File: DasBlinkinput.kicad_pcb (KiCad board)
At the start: 4 copper layers, 25.4 x 50.8 mm, 30 parts, among them P101 CONN_01X02, P102 CONN_01X01, P103 CONN_01X01, P104 CONN_01X01, P105 CONN_01X05, U101 LP2980, U201 MCP6404, U202 LM339

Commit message: added labels to silkscreen
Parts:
- REF V: renamed from P104
- renumbered P102 to +3V, P103 to GND, P101 to PWR
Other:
- board text added: "CH 1"
- board text added: "CH 2"
- board text added: "CH 3"
- board text added: "CH 4"
- board text added: "GND"
- board text added: "Input Voltage: +2V to +16V"
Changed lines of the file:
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@@
 (kicad_pcb (version 4) (host pcbnew 4.0.2-stable)
   (general
-    (links 0)
+    (links 70)
     (no_connects 0)
-    (area 130.480999 65.710999 156.031001 116.661001)
+    (area 130.480999 62.909666 158.502134 119.589333)
     (thickness 1.6)
-    (drawings 5)
+    (drawings 15)
     (tracks 249)
     (zones 0)
@@
     (tags "capacitor 0805")
     (attr smd)
-    (fp_text reference C203 (at 0.254 -1.778 180) (layer B.SilkS)
+    (fp_text reference C203 (at -0.0508 1.8288 180) (layer B.SilkS)
       (effects (font (size 1 1) (thickness 0.15)) (justify mirror))
     )
@@
     (tags "capacitor 0805")
     (attr smd)
-    (fp_text reference C301 (at 0 -1.397 180) (layer F.SilkS)
+    (fp_text reference C301 (at 0 -1.778 180) (layer F.SilkS)
       (effects (font (size 1 1) (thickness 0.15)))
     )
@@
     (descr "Through hole pin header")
     (tags "pin header")
-    (fp_text reference P101 (at 0.0508 -3.4544 180) (layer F.SilkS)
+    (fp_text reference PWR (at 1.143 -3.429 180) (layer F.SilkS)
       (effects (font (size 1 1) (thickness 0.15)))
     )
@@
     (descr "Through hole pin header")
     (tags "pin header")
-    (fp_text reference P102 (at 0 -2.794) (layer F.SilkS)
+    (fp_text reference +3V (at 0 -2.794) (layer F.SilkS)
       (effects (font (size 1 1) (thickness 0.15)))
     )
@@
     (descr "Through hole pin header")
     (tags "pin header")
-    (fp_text reference P103 (at 0 -2.794) (layer F.SilkS)
+    (fp_text reference GND (at -3.556 -0.254) (layer F.SilkS)
       (effects (font (size 1 1) (thickness 0.15)))
     )
@@
     (descr "Through hole pin header")
     (tags "pin header")
-    (fp_text reference P104 (at 3.8608 -0.254 270) (layer F.SilkS)
+    (fp_text reference "REF V" (at 4.191 -0.2286 270) (layer F.SilkS)
       (effects (font (size 1 1) (thickness 0.15)))
     )
@@
     )
   )
+  (gr_text "Input Voltage:\n+2V to +16V" (at 140.843 78.232) (layer B.SilkS)
+    (effects (font (size 1.5 1.5) (thickness 0.3)) (justify mirror))
+  )
+  (gr_text "CH 4" (at 134.366 114.046) (layer F.SilkS)
+    (effects (font (size 1.5 1.5) (thickness 0.3)))
+  )
+  (gr_text "CH 3" (at 134.493 92.837) (layer F.SilkS)
+    (effects (font (size 1.5 1.5) (thickness 0.3)))
+  )
+  (gr_text "CH 2" (at 136.398 90.17) (layer F.SilkS)
+    (effects (font (size 1.5 1.5) (thickness 0.3)))
+  )
+  (gr_text "CH 1" (at 135.255 76.454) (layer F.SilkS)
+    (effects (font (size 1.5 1.5) (thickness 0.3)))
+  )
+  (gr_text "CH 4" (at 146.05 109.474 90) (layer F.SilkS)
+    (effects (font (size 1.5 1.5) (thickness 0.3)))
+  )
+  (gr_text "CH 3" (at 148.59 109.474 90) (layer F.SilkS)
+    (effects (font (size 1.5 1.5) (thickness 0.3)))
+  )
+  (gr_text "CH 2" (at 151.13 109.474 90) (layer F.SilkS)
+    (effects (font (size 1.5 1.5) (thickness 0.3)))
+  )
+  (gr_text "CH 1" (at 153.67 109.474 90) (layer F.SilkS)
+    (effects (font (size 1.5 1.5) (thickness 0.3)))
+  )
+  (gr_text GND (at 143.256 109.982 90) (layer F.SilkS)
+    (effects (font (size 1.5 1.5) (thickness 0.3)))
+  )
   (gr_line (start 130.556 116.586) (end 155.956 116.586) (angle 90) (layer Edge.Cuts) (width 0.15))

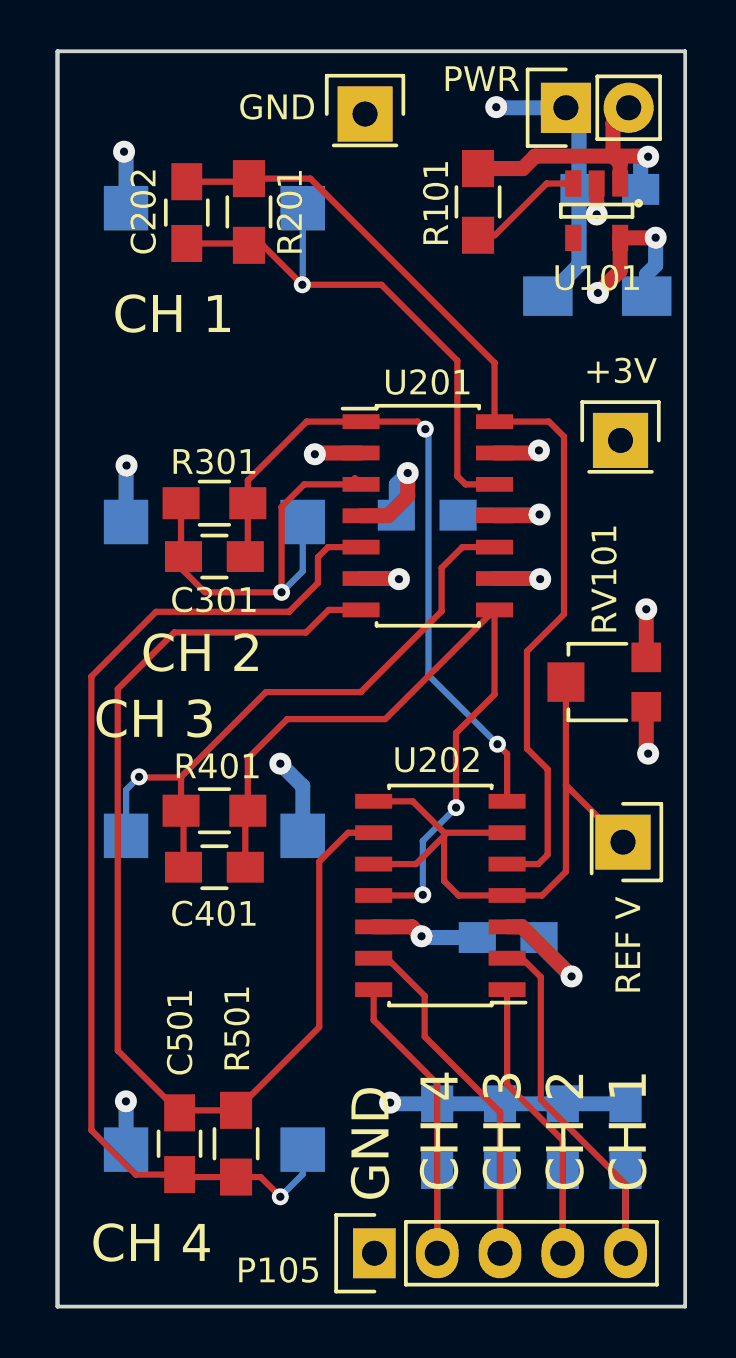
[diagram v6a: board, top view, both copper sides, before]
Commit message: added test points at outputs of op-amps
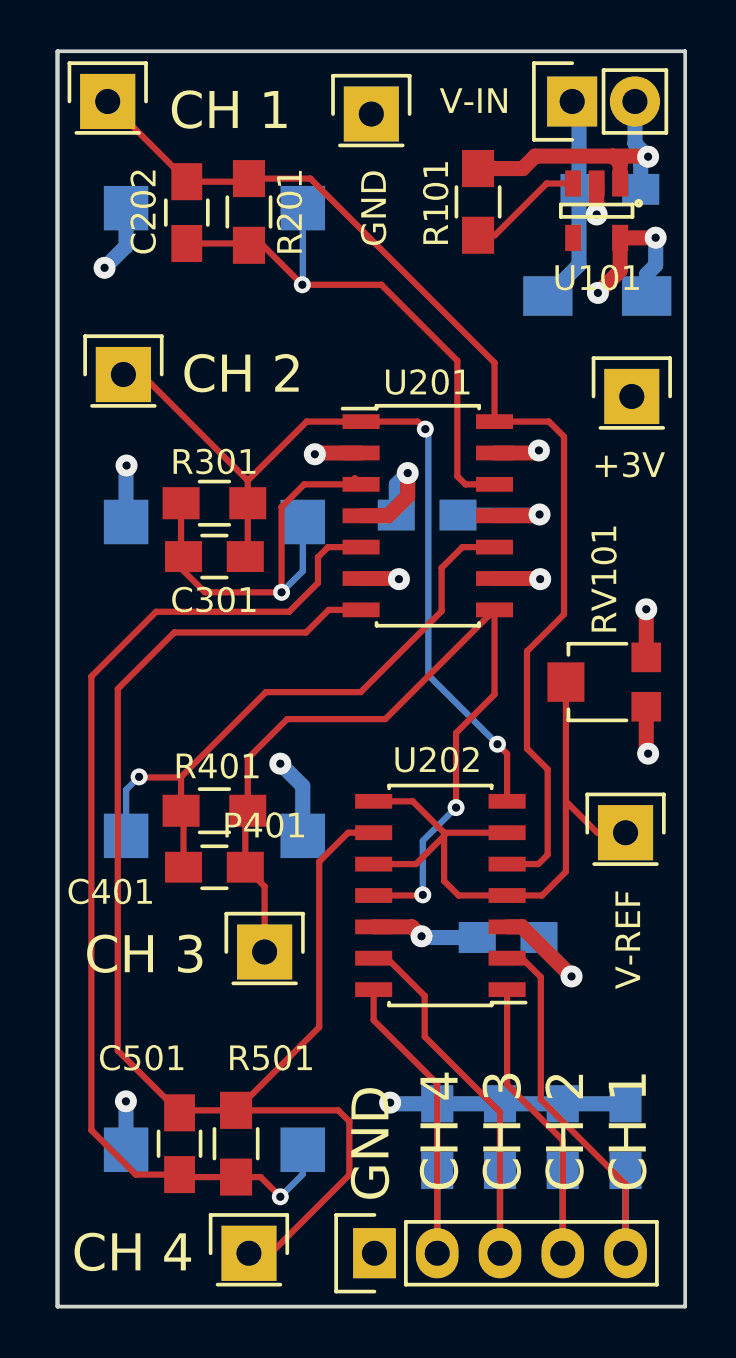
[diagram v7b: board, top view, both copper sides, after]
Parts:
- removed PWR: CONN_01X02, Pin_Headers:Pin_Header_Straight_1x02
- removed REF V: CONN_01X01, Pin_Headers:Pin_Header_Straight_1x01
- added P201: CONN_01X01, Pin_Headers:Pin_Header_Straight_1x01, F.Cu at (132.6, 67.8)
- added P301: CONN_01X01, Pin_Headers:Pin_Header_Straight_1x01, F.Cu at (133.2, 78.9)
- added P401: CONN_01X01, Pin_Headers:Pin_Header_Straight_1x01, F.Cu at (138.9, 102.2)
- added P501: CONN_01X01, Pin_Headers:Pin_Header_Straight_1x01, F.Cu at (138.3, 114.4)
- added V-IN: CONN_01X02, Pin_Headers:Pin_Header_Straight_1x02, F.Cu at (151.4, 67.8)
- added V-REF: CONN_01X01, Pin_Headers:Pin_Header_Straight_1x01, F.Cu at (153.5, 97.4)
- C202, C301, C401, C501: value 50p -> 100p
- PD201, PD301, PD401, PD501: value VBPW34S -> BPW 34 S-Z
- R201, R301, R401, R501: value 2M -> 1M
- moved +3V 1.84 mm to (153.8, 79.8)
- moved GND 0.25 mm to (143.3, 68.3)
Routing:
- net Net-(C501-Pad1): track 45.8 -> 58.1 mm
- net Net-(C301-Pad1): track 29.1 -> 36.0 mm
- net Net-(C202-Pad1): track 40.8 -> 45.4 mm
- net Net-(C401-Pad1): track 31.7 -> 35.4 mm
- net GND: track 40.9 -> 38.7 mm, vias 13 -> 12
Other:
- board text added: "Input Voltage: +3.2V to +16V"
- board text removed: "Input Voltage: +2V to +16V"

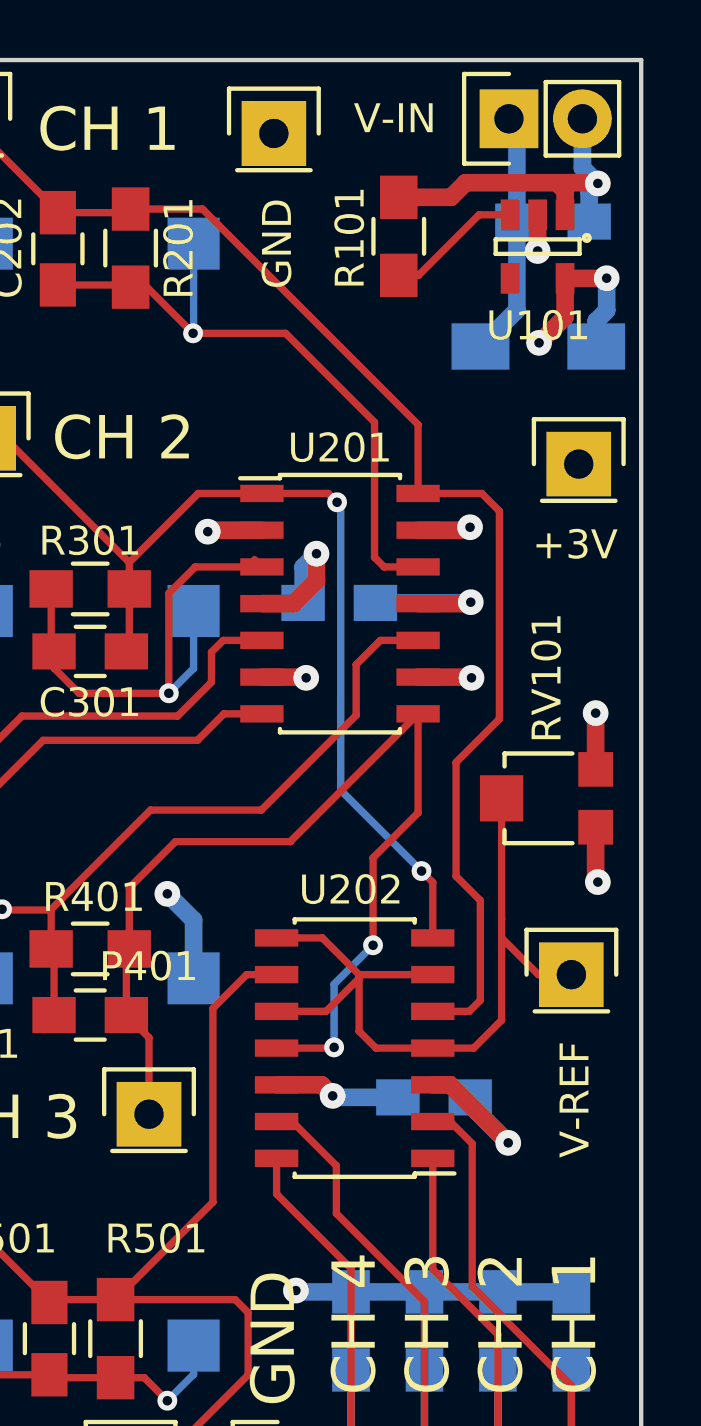
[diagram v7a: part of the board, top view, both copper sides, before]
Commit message: modified labels to be indepenent of footprints
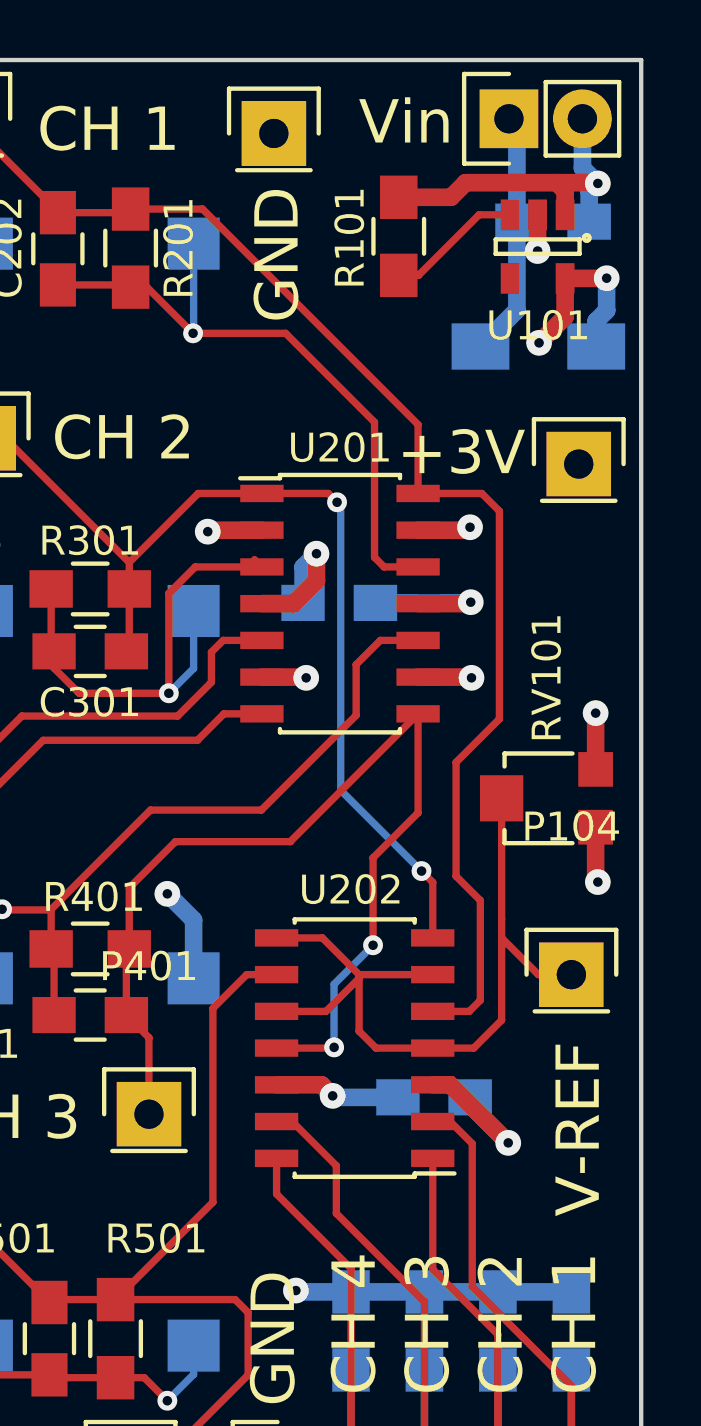
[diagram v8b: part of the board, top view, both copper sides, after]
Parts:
- removed +3V, GND, V-REF: CONN_01X01, Pin_Headers:Pin_Header_Straight_1x01
- removed V-IN: CONN_01X02, Pin_Headers:Pin_Header_Straight_1x02
- added P101: CONN_01X02, Pin_Headers:Pin_Header_Straight_1x02, F.Cu at (151.4, 67.8)
- added P102: CONN_01X01, Pin_Headers:Pin_Header_Straight_1x01, F.Cu at (153.8, 79.8)
- added P103: CONN_01X01, Pin_Headers:Pin_Header_Straight_1x01, F.Cu at (143.3, 68.3)
- added P104: CONN_01X01, Pin_Headers:Pin_Header_Straight_1x01, F.Cu at (153.5, 97.4)
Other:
- board text added: "+3V"
- board text added: "V-REF"
- board text added: "Vin"
